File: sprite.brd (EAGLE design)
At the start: 35 x 35 mm, 41 parts

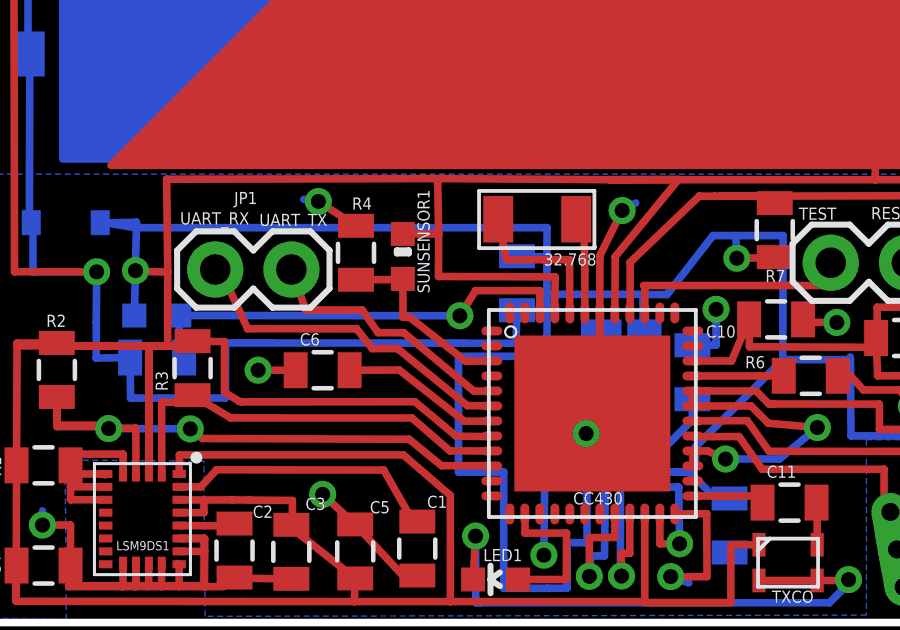
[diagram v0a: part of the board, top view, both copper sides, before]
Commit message: spaced out resistor
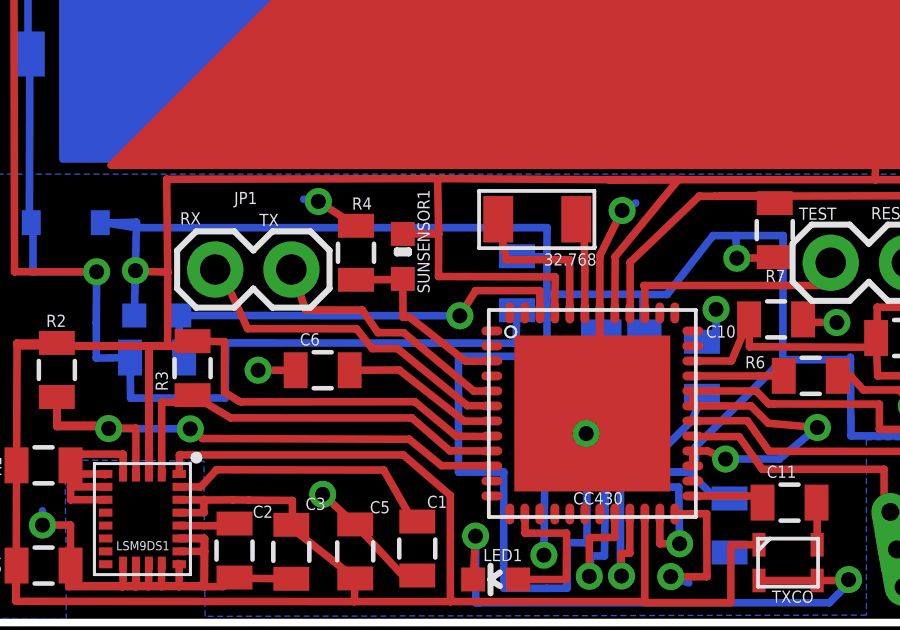
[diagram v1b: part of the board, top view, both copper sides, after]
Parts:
- moved R8 0.34 mm to (24.0, 8.46)
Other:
- board text added: "RX"
- board text added: "TX"
- board text removed: "UART_RX"
- board text removed: "UART_TX"
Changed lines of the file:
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@@
 <grid distance="0.000000123031" unitdist="inch" unit="inch" style="lines" multiple="1" display="no" altdistance="0.025" altunitdist="inch" altunit="mm"/>
 <layers>
-<layer number="1" name="Top" color="4" fill="1" visible="yes" active="yes"/>
-<layer number="2" name="Route2" color="1" fill="3" visible="yes" active="yes"/>
+<layer number="1" name="Top" color="4" fill="1" visible="no" active="yes"/>
+<layer number="2" name="Route2" color="1" fill="3" visible="no" active="yes"/>
 <layer number="3" name="Route3" color="4" fill="3" visible="no" active="no"/>
 <layer number="14" name="Route14" color="1" fill="6" visible="no" active="no"/>
-<layer number="15" name="Route15" color="4" fill="6" visible="yes" active="yes"/>
+<layer number="15" name="Route15" color="4" fill="6" visible="no" active="yes"/>
 <layer number="16" name="Bottom" color="1" fill="1" visible="yes" active="yes"/>
 <layer number="17" name="Pads" color="2" fill="1" visible="yes" active="yes"/>
@@
 <layer number="19" name="Unrouted" color="6" fill="1" visible="yes" active="yes"/>
 <layer number="20" name="Dimension" color="15" fill="1" visible="yes" active="yes"/>
-<layer number="21" name="tPlace" color="7" fill="1" visible="yes" active="yes"/>
+<layer number="21" name="tPlace" color="7" fill="1" visible="no" active="yes"/>
 <layer number="22" name="bPlace" color="7" fill="1" visible="no" active="yes"/>
 <layer number="23" name="tOrigins" color="15" fill="1" visible="no" active="yes"/>
@@
 <layer number="43" name="vRestrict" color="2" fill="10" visible="no" active="yes"/>
 <layer number="44" name="Drills" color="7" fill="1" visible="no" active="yes"/>
-<layer number="45" name="Holes" color="7" fill="1" visible="yes" active="yes"/>
+<layer number="45" name="Holes" color="7" fill="1" visible="no" active="yes"/>
 <layer number="46" name="Milling" color="3" fill="1" visible="no" active="yes"/>
 <layer number="47" name="Measures" color="7" fill="1" visible="no" active="yes"/>
@@
 <wire x1="0" y1="35" x2="0" y2="0" width="0.254" layer="20"/>
 <hole x="32.1" y="32.1" drill="2.8"/>
-<text x="6.61" y="13.27025" size="0.4064" layer="21">UART_RX</text>
-<text x="9.252546875" y="13.21736875" size="0.4064" layer="21">UART_TX</text>
+<text x="6.61" y="13.27025" size="0.4064" layer="21">RX</text>
+<text x="9.252546875" y="13.21736875" size="0.4064" layer="21">TX</text>
 <text x="27.239675" y="13.424815625" size="0.4064" layer="21">TEST</text>
 <text x="29.64264375" y="13.443159375" size="0.4064" layer="21">RESET</text>
@@
 </element>
 <element name="C11" library="SparkFun" package="0805" value="10nF" x="26.92746875" y="3.9971"/>
-<element name="R8" library="SparkFun" package="0805" value="20" x="23.686975" y="8.343" smashed="yes" rot="MR270">
-<attribute name="NAME" x="25.4672625" y="8.795396875" size="0.4064" layer="26" rot="MR270"/>
-<attribute name="VALUE" x="25.083975" y="9.359" size="0.4064" layer="28" rot="MR270"/>
+<element name="R8" library="SparkFun" package="0805" value="20" x="24.007671875" y="8.458134375" smashed="yes" rot="MR270">
+<attribute name="NAME" x="25.787959375" y="8.91053125" size="0.4064" layer="26" rot="MR270"/>
+<attribute name="VALUE" x="25.404671875" y="9.474134375" size="0.4064" layer="28" rot="MR270"/>
 </element>
 <element name="C12" library="SparkFun" package="0805" value="10uF" x="24.9302" y="3.234571875" rot="MR90"/>
@@
 <wire x1="18.2776" y1="15.128875" x2="18.2776" y2="2.4276875" width="0.254" layer="2"/>
 <contactref element="R8" pad="1"/>
-<wire x1="23.686975" y1="9.243" x2="24.4782125" y2="9.243" width="0.254" layer="16"/>
+<wire x1="24.007671875" y1="9.358134375" x2="24.4782125" y2="9.243" width="0.254" layer="16"/>
 <wire x1="24.4782125" y1="9.243" x2="24.4782125" y2="10.441328125" width="0.254" layer="16"/>
 </signal>
@@
 <contactref element="H-BRIDGE" pad="OUT2"/>
 <contactref element="R8" pad="2"/>
-<wire x1="23.686975" y1="7.443" x2="23.686975" y2="6.750084375" width="0.254" layer="16"/>
+<wire x1="24.007671875" y1="7.558134375" x2="23.686975" y2="6.750084375" width="0.254" layer="16"/>
 <wire x1="23.686975" y1="6.750084375" x2="22.45015" y2="5.513259375" width="0.254" layer="16"/>
 <wire x1="22.4480125" y1="5.515396875" x2="22.45015" y2="5.513259375" width="0.254" layer="16"/>

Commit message: updated gerbers
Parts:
- added R9: 5.6K, SparkFun:0805
- D1: value 2.7V -> 2.2V
- R8: value 20 -> 1K
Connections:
- new net N$6: R9.1, VCCPIN.PIN
- net VCC: now also R9.2; no longer VCCPIN.PIN
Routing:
- net VCC: track 373.2 -> 366.8 mm
- net N$6: track 0.00 -> 4.99 mm
